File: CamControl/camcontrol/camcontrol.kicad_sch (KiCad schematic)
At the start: 65 parts, among them J1 Power 1, J2 USB_B_Micro, J3 Power 1, J4 Power 1, J5 Conn_01x02, J6 Conn_01x02, J7 Power 1, J8 Conn_01x03, Q1 AO3401A, Q2 AO3401A, Q3 AO3401A, Q4 AO3401A, U1 E22-900MM22S, U2 TPS1HC30BQPWPRQ1, U4 XC6206P332MR, U5 W25Q128JVS, U6 RP2040, U7 TPS1HC30BQPWPRQ1, X1 SX1M12.000M10F30TNN

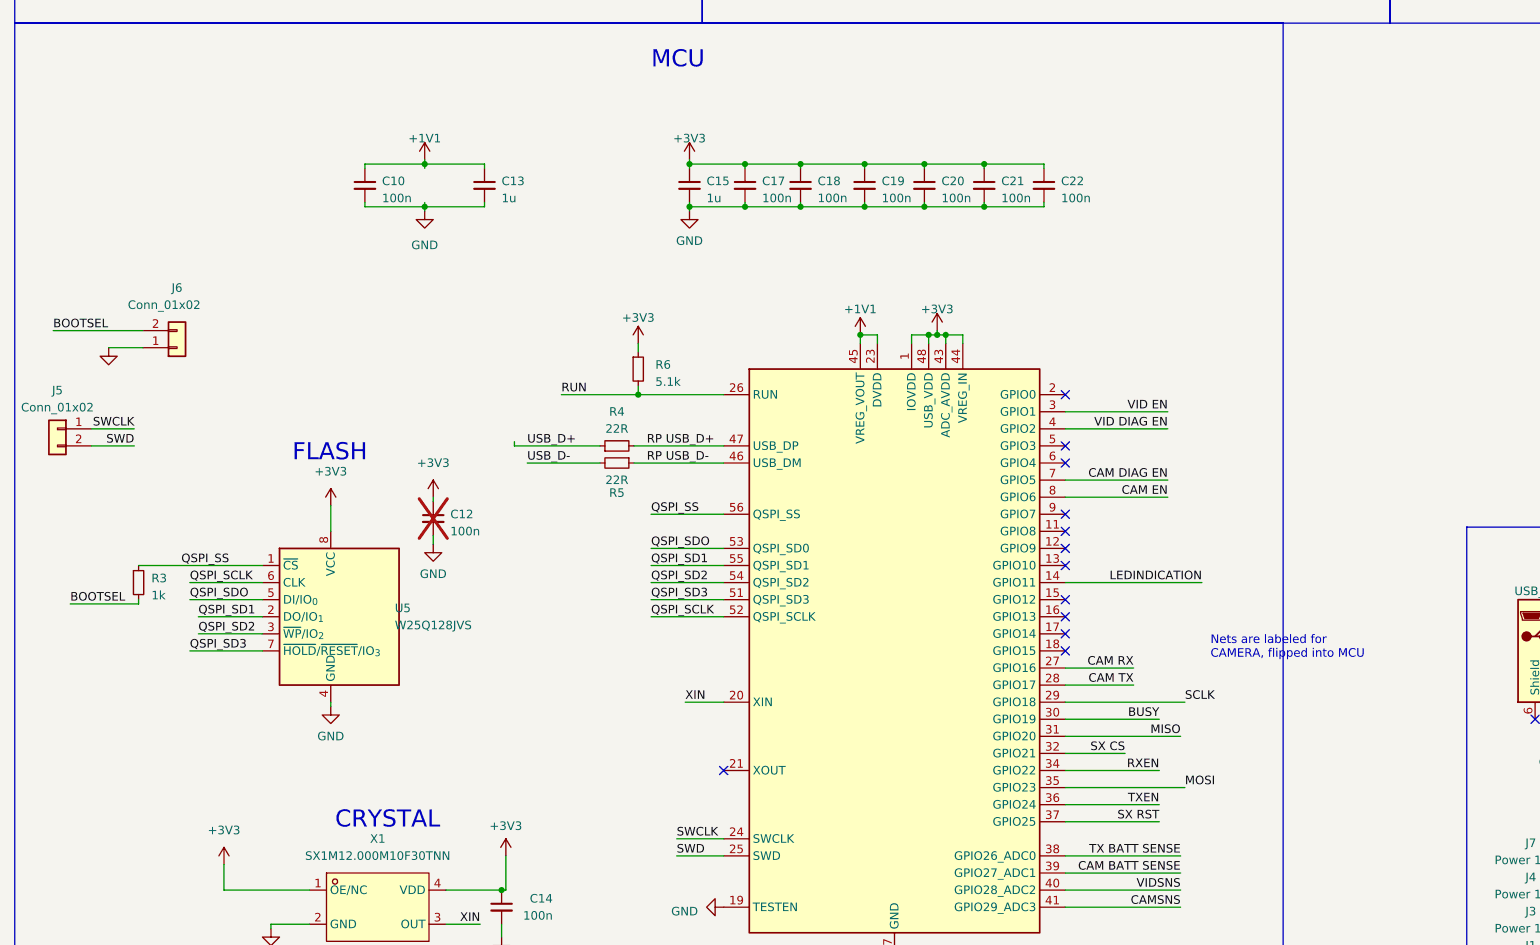
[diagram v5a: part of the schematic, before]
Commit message: camcontrol stm32
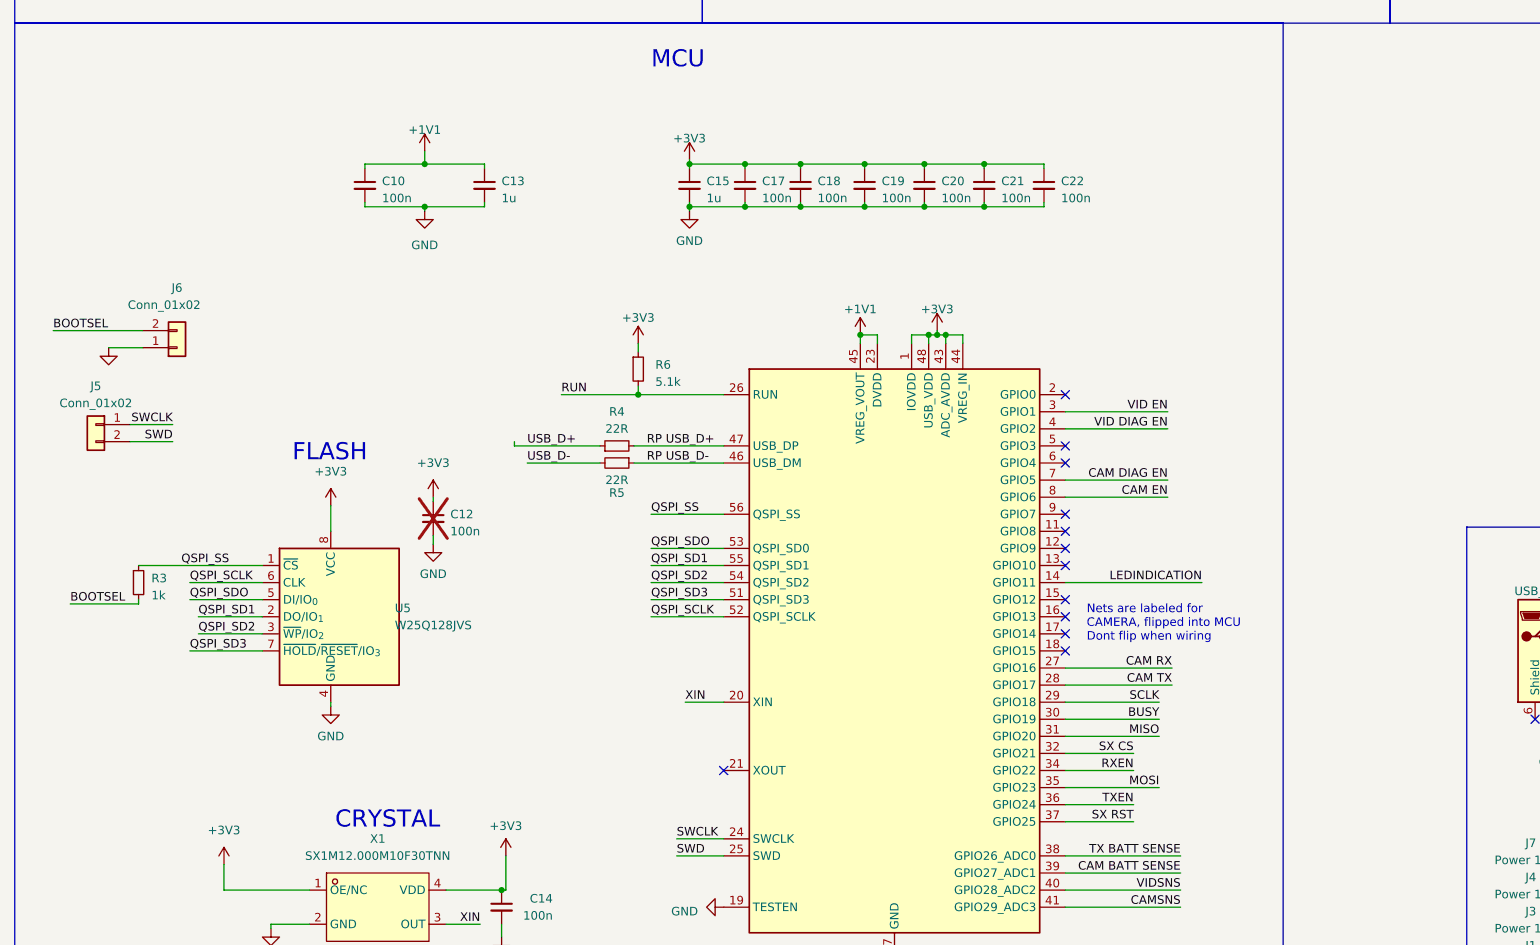
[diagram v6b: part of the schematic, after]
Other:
- note added: "Nets are labeled for CAMERA, flipped into MCU Dont flip when wiring"
- note removed: "Nets are labeled for CAMERA, flipped into MCU"
- moved on the sheet: J5
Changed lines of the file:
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@@
 		)
 	)
-	(text "Nets are labeled for \nCAMERA, flipped into MCU"
+	(text "Nets are labeled for \nCAMERA, flipped into MCU\nDont flip when wiring"
 		(exclude_from_sim no)
-		(at 189.865 194.945 0)
+		(at 171.45 192.405 0)
 		(effects
 			(font
@@
 	)
 	(junction
-		(at 73.025 121.285)
-		(diameter 0)
-		(color 0 0 0 0)
-	)
-	(junction
 		(at 150.495 74.295)
 		(diameter 0)
@@
 	)
 	(junction
+		(at 73.025 121.285)
+		(diameter 0)
+		(color 0 0 0 0)
+	)
+	(junction
 		(at 254 37.465)
 		(diameter 0)
@@
 	(wire
 		(pts
-			(xy 168.275 219.075) (xy 182.245 219.075)
+			(xy 168.275 219.075) (xy 178.435 219.075)
 		)
 		(stroke
@@
 	(wire
 		(pts
-			(xy 178.435 196.215) (xy 168.275 196.215)
+			(xy 184.15 196.215) (xy 168.275 196.215)
 		)
 		(stroke
@@
 	(wire
 		(pts
-			(xy 178.435 198.755) (xy 168.275 198.755)
+			(xy 184.15 198.755) (xy 168.275 198.755)
 		)
 		(stroke
@@
 	(wire
 		(pts
-			(xy 168.275 208.915) (xy 177.165 208.915)
+			(xy 168.275 208.915) (xy 178.435 208.915)
 		)
 		(stroke
@@
 	(wire
 		(pts
-			(xy 73.025 121.285) (xy 81.915 121.285)
+			(xy 64.135 121.285) (xy 73.025 121.285)
 		)
 		(stroke
@@
 	(wire
 		(pts
-			(xy 73.025 120.65) (xy 73.025 121.285)
+			(xy 73.025 119.38) (xy 73.025 121.285)
 		)
 		(stroke
@@
 	(wire
 		(pts
-			(xy 168.275 206.375) (xy 185.42 206.375)
+			(xy 168.275 206.375) (xy 182.245 206.375)
 		)
 		(stroke
@@
 	(wire
 		(pts
-			(xy 64.135 121.285) (xy 73.025 121.285)
-		)
-		(stroke
-			(width 0)
-			(type default)
-		)
-	)
-	(wire
-		(pts
 			(xy 358.14 221.615) (xy 363.22 221.615)
 		)
@@
 	(wire
 		(pts
-			(xy 73.025 121.285) (xy 73.025 121.92)
-		)
-		(stroke
-			(width 0)
-			(type default)
-		)
-	)
-	(wire
-		(pts
 			(xy 199.39 44.45) (xy 195.58 44.45)
 		)
@@
 	(wire
 		(pts
-			(xy 168.275 213.995) (xy 186.055 213.995)
+			(xy 168.275 213.995) (xy 182.245 213.995)
 		)
 		(stroke
@@
 	(wire
 		(pts
+			(xy 73.025 121.285) (xy 81.915 121.285)
+		)
+		(stroke
+			(width 0)
+			(type default)
+		)
+	)
+	(wire
+		(pts
 			(xy 67.945 267.97) (xy 98.425 267.97)
 		)
@@
 	(wire
 		(pts
-			(xy 182.245 216.535) (xy 168.275 216.535)
+			(xy 178.435 216.535) (xy 168.275 216.535)
 		)
 		(stroke
@@
 	(wire
 		(pts
-			(xy 23.495 163.195) (xy 29.845 163.195)
+			(xy 29.21 162.56) (xy 35.56 162.56)
 		)
 		(stroke
@@
 	(wire
 		(pts
-			(xy 182.245 211.455) (xy 168.275 211.455)
+			(xy 178.435 211.455) (xy 168.275 211.455)
 		)
 		(stroke
@@
 	(wire
 		(pts
-			(xy 73.025 127.635) (xy 73.025 127)
-		)
-		(stroke
-			(width 0)
-			(type default)
-		)
-	)
-	(wire
-		(pts
 			(xy 142.875 40.64) (xy 142.875 41.91)
 		)
@@
 	(wire
 		(pts
-			(xy 23.495 160.655) (xy 29.845 160.655)
+			(xy 29.21 160.02) (xy 35.56 160.02)
 		)
 		(stroke
@@
 	(wire
 		(pts
-			(xy 168.275 201.295) (xy 186.055 201.295)
+			(xy 168.275 201.295) (xy 182.245 201.295)
 		)
 		(stroke
@@
 	)
 	(label "SWCLK"
-		(at 29.845 160.655 180)
+		(at 35.56 160.02 180)
 		(effects
 			(font
@@
 	)
 	(label "SCLK"
-		(at 186.055 201.295 0)
+		(at 182.245 201.295 180)
 		(effects
 			(font
 				(size 1.27 1.27)
 			)
-			(justify left bottom)
+			(justify right bottom)
 		)
 	)
@@
 	)
 	(label "MOSI"
-		(at 186.055 213.995 0)
+		(at 182.245 213.995 180)
 		(effects
 			(font
 				(size 1.27 1.27)
 			)
-			(justify left bottom)
+			(justify right bottom)
 		)
 	)
@@
 	)
 	(label "CAM TX"
-		(at 178.435 198.755 180)
+		(at 184.15 198.755 180)
 		(effects
 			(font
@@
 	)
 	(label "MISO"
-		(at 185.42 206.375 180)
+		(at 182.245 206.375 180)
 		(effects
 			(font
@@
 	)
 	(label "TXEN"
-		(at 182.245 216.535 180)
+		(at 178.435 216.535 180)
 		(effects
 			(font
@@
 	)
 	(label "SX RST"
-		(at 182.245 219.075 180)
+		(at 178.435 219.075 180)
 		(effects
 			(font
@@
 	)
 	(label "RXEN"
-		(at 182.245 211.455 180)
+		(at 178.435 211.455 180)
 		(effects
 			(font
@@
 	)
 	(label "CAM RX"
-		(at 178.435 196.215 180)
+		(at 184.15 196.215 180)
 		(effects
 			(font
@@
 	)
 	(label "SWD"
-		(at 29.845 163.195 180)
+		(at 35.56 162.56 180)
 		(effects
 			(font
@@
 	)
 	(label "SX CS"
-		(at 177.165 208.915 180)
+		(at 178.435 208.915 180)
 		(effects
 			(font
@@
 	(symbol
 		(lib_id "Connector_Generic:Conn_01x02")
-		(at 18.415 160.655 0)
+		(at 24.13 160.02 0)
 		(mirror y)
 		(unit 1)
@@
 		(dnp no)
 		(property "Reference" "J5"
-			(at 18.415 154.94 0)
+			(at 24.13 154.305 0)
 			(effects
 				(font
@@
 		)
 		(property "Value" "Conn_01x02"
-			(at 18.415 157.48 0)
+			(at 24.13 156.845 0)
 			(effects
 				(font
@@
 		)
 		(property "Footprint" "Jumper:SolderJumper-2_P1.3mm_Open_Pad1.0x1.5mm"
-			(at 20.32 166.37 0)
+			(at 26.035 165.735 0)
 			(effects
 				(font
@@
 		)
 		(property "Datasheet" "~"
-			(at 18.415 160.655 0)
+			(at 24.13 160.02 0)
 			(effects
 				(font
@@
 		)
 		(property "Description" "Generic connector, single row, 01x02, script generated (kicad-library-utils/schlib/autogen/connector/)"
-			(at 18.415 160.655 0)
+			(at 24.13 160.02 0)
 			(effects
 				(font
@@
 	(symbol
 		(lib_id "power:+1V1")
-		(at 73.025 120.65 0)
+		(at 73.025 119.38 0)
 		(unit 1)
 		(exclude_from_sim no)
@@
 		(fields_autoplaced yes)
 		(property "Reference" "#PWR030"
-			(at 73.025 124.46 0)
+			(at 73.025 123.19 0)
 			(effects
 				(font
@@
 		)
 		(property "Value" "+1V1"
-			(at 73.025 117.475 0)
+			(at 73.025 116.205 0)
 			(effects
 				(font
@@
 		)
 		(property "Footprint" ""
-			(at 73.025 120.65 0)
+			(at 73.025 119.38 0)
 			(effects
 				(font
@@
 		)
 		(property "Datasheet" ""
-			(at 73.025 120.65 0)
+			(at 73.025 119.38 0)
 			(effects
 				(font
@@
 		)
 		(property "Description" "Power symbol creates a global label with name \"+1V1\""
-			(at 73.025 120.65 0)
+			(at 73.025 119.38 0)
 			(effects
 				(font
